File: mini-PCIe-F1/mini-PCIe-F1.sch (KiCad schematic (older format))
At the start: 1 part

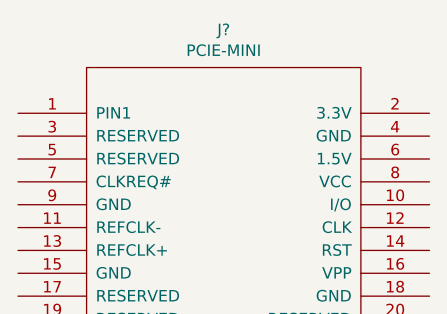
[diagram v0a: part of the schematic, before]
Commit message: Fixes connector placement in F1 template
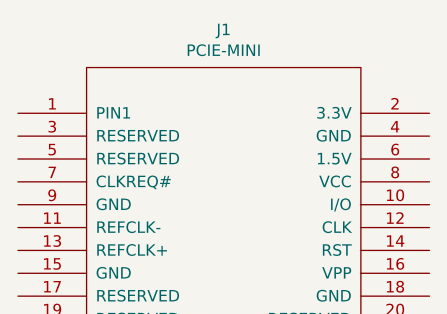
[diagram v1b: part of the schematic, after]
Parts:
- J1: renamed from J?; footprint MODULE -> mini-PCIe:miniPCIeConn
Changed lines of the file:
@@
 $EndDescr
 $Comp
-L mini-PCIe:PCIE-MINI J?
+L mini-PCIe:PCIE-MINI J1
 U 1 1 602A6AB9
 P 2100 2700
-F 0 "J?" H 2100 4315 50  0000 C CNN
+F 0 "J1" H 2100 4315 50  0000 C CNN
 F 1 "PCIE-MINI" H 2100 4224 50  0000 C CNN
-F 2 "MODULE" H 2100 2700 50  0001 C CNN
+F 2 "mini-PCIe:miniPCIeConn" H 2100 2700 50  0001 C CNN
 F 3 "DOCUMENTATION" H 2100 1300 50  0001 C CNN
 	1    2100 2700
